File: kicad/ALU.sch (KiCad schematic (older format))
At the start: 7 parts, among them U1 74LS86, U2 74LS86, U3 74LS283, U4 74LS283, U46 7402, U47 74LS08, U5 74LS245

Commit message: bugfixed design
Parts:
- renumbered U46 to U5, U5 to U6, U47 to U7
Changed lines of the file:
@@
 LIBS:valves
 LIBS:switches
-LIBS:74xxx
-LIBS:28c16
 LIBS:sap-be-cache
-EELAYER 24 0
+EELAYER 25 0
 EELAYER END
 $Descr A4 11693 8268
@@
 $EndComp
 $Comp
-L 74LS245 U5
+L 74LS245 U6
 U 1 1 590CA27C
 P 7150 4650
-F 0 "U5" H 7250 5225 50  0000 L BNN
+F 0 "U6" H 7250 5225 50  0000 L BNN
 F 1 "74LS245" H 7200 4075 50  0000 L TNN
 F 2 "Housings_DIP:DIP-20_W7.62mm_LongPads" H 7150 4650 50  0001 C CNN
@@
 $EndComp
 $Comp
-L VCC #PWR011
+L VCC #PWR9
 U 1 1 590D04F1
 P 6350 5050
-F 0 "#PWR011" H 6350 4900 50  0001 C CNN
+F 0 "#PWR9" H 6350 4900 50  0001 C CNN
 F 1 "VCC" H 6350 5200 50  0000 C CNN
 F 2 "" H 6350 5050 50  0000 C CNN
@@
 	1700 3000 1800 3100
 $Comp
-L 7402 U46
+L 7402 U5
 U 1 1 5ACC3884
 P 7050 1200
-F 0 "U46" H 7050 1250 50  0000 C CNN
+F 0 "U5" H 7050 1250 50  0000 C CNN
 F 1 "7402" H 7100 1150 50  0000 C CNN
 F 2 "" H 7050 1200 50  0000 C CNN
@@
 $EndComp
 $Comp
-L 7402 U46
+L 7402 U5
 U 2 1 5ACC3898
 P 7050 1700
-F 0 "U46" H 7050 1750 50  0000 C CNN
+F 0 "U5" H 7050 1750 50  0000 C CNN
 F 1 "7402" H 7100 1650 50  0000 C CNN
 F 2 "" H 7050 1700 50  0000 C CNN
@@
 $EndComp
 $Comp
-L 7402 U46
+L 7402 U5
 U 3 1 5ACC38AC
 P 7050 2250
-F 0 "U46" H 7050 2300 50  0000 C CNN
+F 0 "U5" H 7050 2300 50  0000 C CNN
 F 1 "7402" H 7100 2200 50  0000 C CNN
 F 2 "" H 7050 2250 50  0000 C CNN
@@
 $EndComp
 $Comp
-L 7402 U46
+L 7402 U5
 U 4 1 5ACC38C0
 P 7050 2750
-F 0 "U46" H 7050 2800 50  0000 C CNN
+F 0 "U5" H 7050 2800 50  0000 C CNN
 F 1 "7402" H 7100 2700 50  0000 C CNN
 F 2 "" H 7050 2750 50  0000 C CNN
@@
 $EndComp
 $Comp
-L 74LS08 U47
+L 74LS08 U7
 U 1 1 5ACC38D4
 P 8450 1450
-F 0 "U47" H 8450 1500 50  0000 C CNN
+F 0 "U7" H 8450 1500 50  0000 C CNN
 F 1 "74LS08" H 8450 1400 50  0000 C CNN
 F 2 "" H 8450 1450 50  0000 C CNN
@@
 $EndComp
 $Comp
-L 74LS08 U47
+L 74LS08 U7
 U 3 1 5ACC38FC
 P 9850 1950
-F 0 "U47" H 9850 2000 50  0000 C CNN
+F 0 "U7" H 9850 2000 50  0000 C CNN
 F 1 "74LS08" H 9850 1900 50  0000 C CNN
 F 2 "" H 9850 1950 50  0000 C CNN
@@
 $EndComp
 $Comp
-L 74LS08 U47
+L 74LS08 U7
 U 2 1 5ACC391A
 P 8450 2500
-F 0 "U47" H 8450 2550 50  0000 C CNN
+F 0 "U7" H 8450 2550 50  0000 C CNN
 F 1 "74LS08" H 8450 2450 50  0000 C CNN
 F 2 "" H 8450 2500 50  0000 C CNN

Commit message: design as built
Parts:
- removed U5: 7402, symbol 7402
- removed U6: 74LS245, Housings_DIP:DIP-20_W7.62mm_LongPads, symbol 74LS245
- removed U7: 74LS08, symbol 74LS08
- added D501, D502, D503, D504, D505, D506, D507, D508: LED, LEDs:LED-5MM, symbol LED
- added RN501: R_Network08, Resistors_ThroughHole:Resistor_Array_SIP9, symbol R_Network08
- added U505: 74LS688, Housings_DIP:DIP-20_W7.62mm_LongPads, symbol 74LS688
- added U506: 74LS244, Housings_DIP:DIP-20_W7.62mm_LongPads, symbol 74LS244
- renumbered U1 to U501, U2 to U502, U3 to U503, U4 to U504
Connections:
- net labels added: GND, ~ZERO
- net labels removed: VCC, ZERO
- wire segments 120 -> 133
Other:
- moved on the sheet: U503, U504

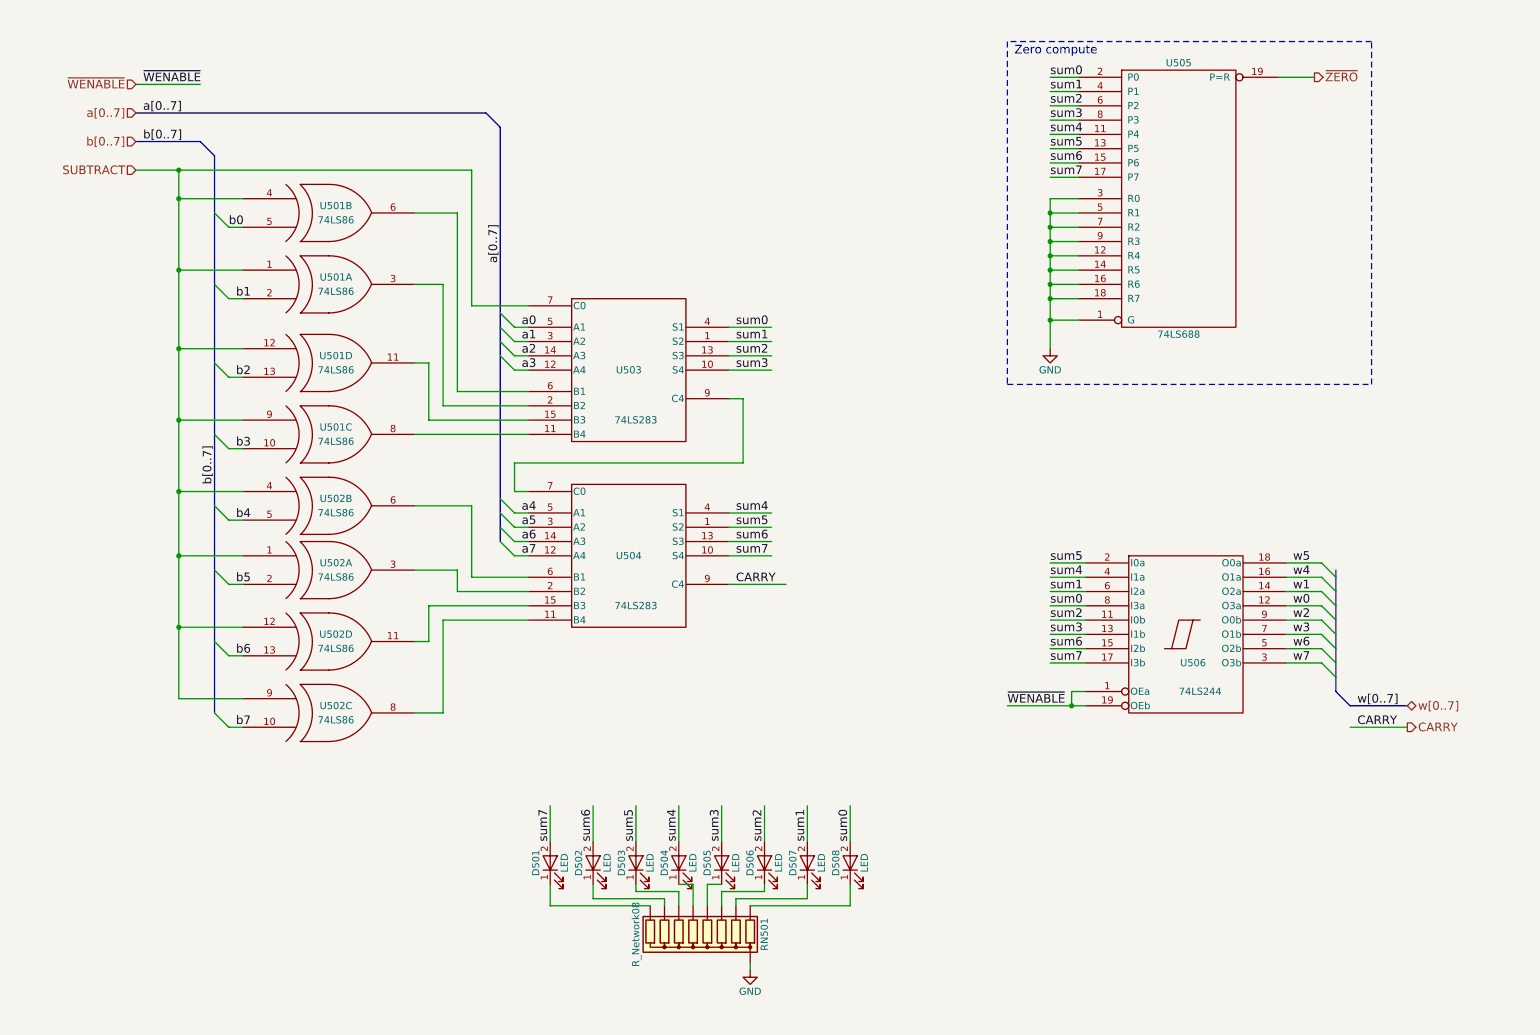
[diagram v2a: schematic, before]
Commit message: Update to current kicad version
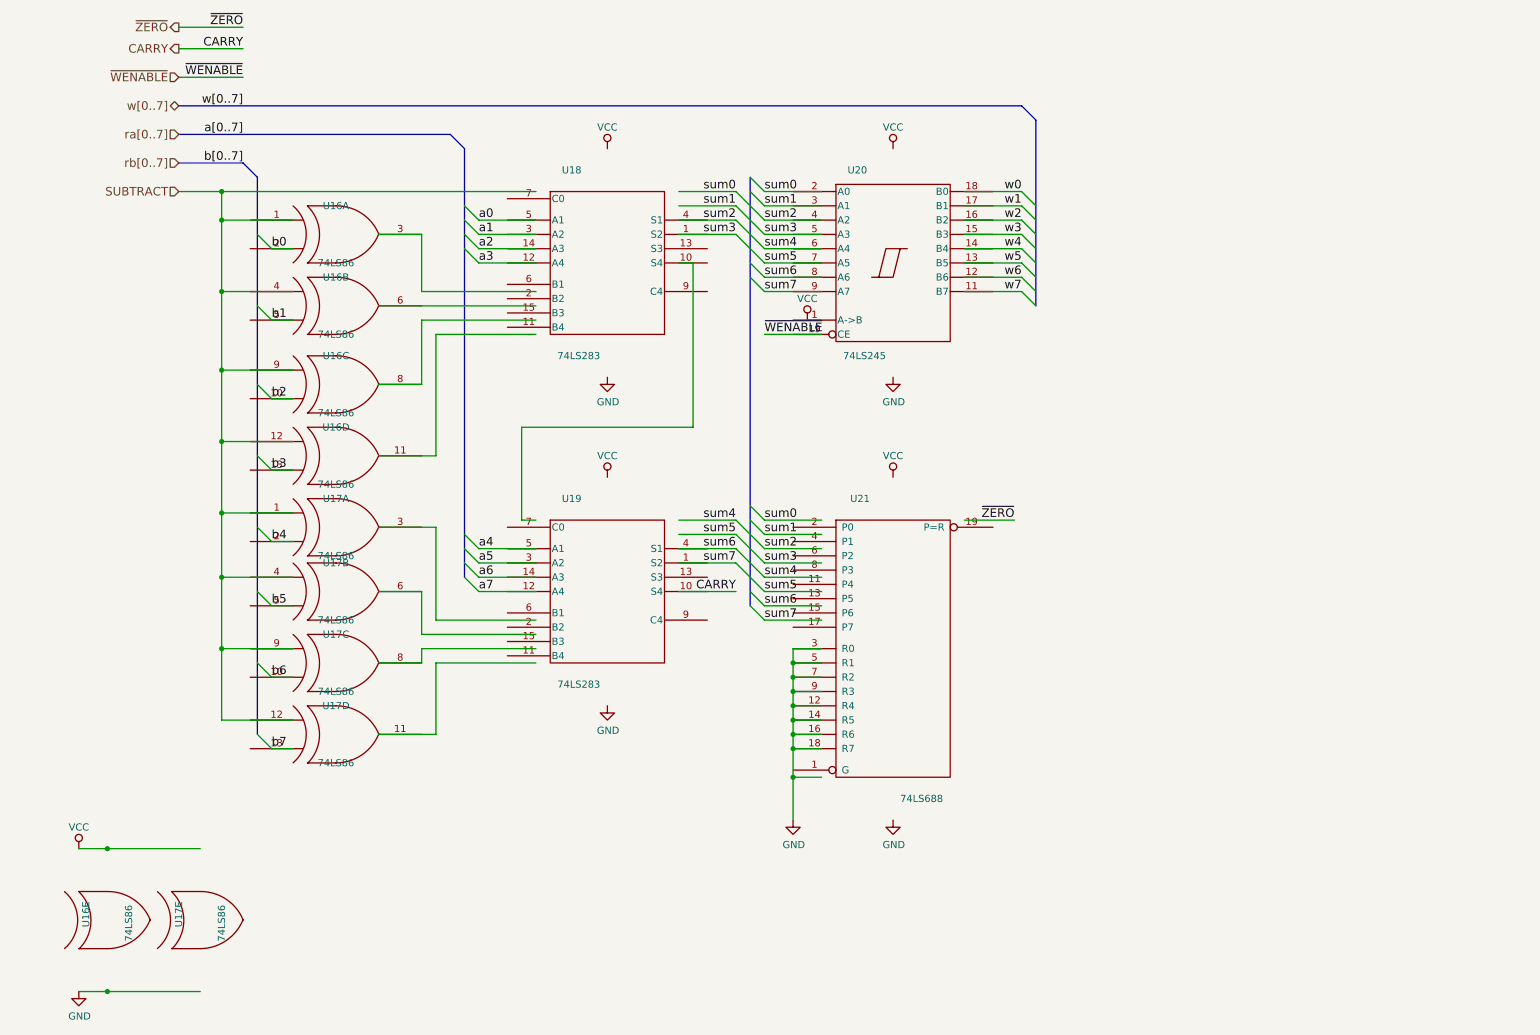
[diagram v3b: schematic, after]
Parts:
- removed D501, D502, D503, D504, D505, D506, D507, D508: LED, LEDs:LED-5MM, symbol LED
- removed RN501: R_Network08, Resistors_ThroughHole:Resistor_Array_SIP9, symbol R_Network08
- removed U501, U502: 74LS86, Housings_DIP:DIP-14_W7.62mm_LongPads, symbol 74LS86
- removed U503, U504: 74LS283, Housings_DIP:DIP-16_W7.62mm_LongPads, symbol 74LS283
- removed U505: 74LS688, Housings_DIP:DIP-20_W7.62mm_LongPads, symbol 74LS688
- removed U506: 74LS244, Housings_DIP:DIP-20_W7.62mm_LongPads, symbol 74LS244
- added U16, U17: 74LS86, symbol 74xx:74LS86
- added U18, U19: 74LS283, symbol 74xx:74LS283
- added U20: 74LS245, symbol 74xx:74LS245
- added U21: 74LS688, symbol 74xx:74LS688
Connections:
- net labels added: VCC, ra[0..7], rb[0..7]
- wire segments 133 -> 122
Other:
- note removed: "Zero compute"
